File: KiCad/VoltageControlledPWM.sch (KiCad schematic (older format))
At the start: 26 parts, among them J1 +12V|GND|-12V, J2 3.3V|5.0V (Output Reference), J3 3.3V | 5.0V Voltage Control, J4 PWM Output, Q1 2N3906, U1 LM393, U2 CA3240E, U3 LM311

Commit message: Latest updates
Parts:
- added TP0: GND, TestPoint:TestPoint_Loop_D2.50mm_Drill1.0mm, symbol Connector:TestPoint
- added TP1: Square Wave, TestPoint:TestPoint_Loop_D2.50mm_Drill1.0mm, symbol Connector:TestPoint
- added TP2: Triange Wave, TestPoint:TestPoint_Loop_D2.50mm_Drill1.0mm, symbol Connector:TestPoint
- added TP3: Sweep, TestPoint:TestPoint_Loop_D2.50mm_Drill1.0mm, symbol Connector:TestPoint
- J1: value +12V|GND|-12V -> -12V | GND | +12V
- J2: value 3.3V|5.0V (Output Reference) -> 3.3V or 5.0V (Output Reference)
- J3: value 3.3V | 5.0V Voltage Control -> 3.3V or 5.0V Voltage Control
- R6: value 500 -> 460
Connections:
- net GND: now also TP0.1
- net at R1.1, R1.2, R3.3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: now also TP1.1
- net at C1.1, R2.1, U2.1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: now also TP2.1
- net at R10.1, U2.7, U3.2 (+): now also TP3.1
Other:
- moved on the sheet: C1, C2, C3, C4, C5, C6, C7, J1, J2, J3, J4, Q1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

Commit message: Updated to the board.
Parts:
- R8: value 20K -> 27K
- R9: value 5K -> 10K
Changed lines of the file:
@@
 Sheet 1 1
 Title "Voltage Controlled PWM"
-Date "2021-07-16"
+Date "2021-07-20"
 Rev "V1.0"
 Comp "TetraSys"
@@
 P 6200 5400
 F 0 "R8" H 6268 5446 50  0000 L CNN
-F 1 "20K" H 6268 5355 50  0000 L CNN
+F 1 "27K" H 6268 5355 50  0000 L CNN
 F 2 "Resistor_THT:R_Axial_DIN0207_L6.3mm_D2.5mm_P10.16mm_Horizontal" H 6200 5400 50  0001 C CNN
 F 3 "~" H 6200 5400 50  0001 C CNN
@@
 P 5900 5200
 F 0 "R9" V 5787 5200 50  0000 C CNN
-F 1 "5K" V 5696 5200 50  0000 C CNN
+F 1 "10K" V 5696 5200 50  0000 C CNN
 F 2 "Potentiometer_THT:Potentiometer_Bourns_3296W_Vertical" H 5900 5200 50  0001 C CNN
 F 3 "~" H 5900 5200 50  0001 C CNN
@@
 $EndComp
 $Comp
-L power:GND #PWR?
+L power:GND #PWR0106
 U 1 1 613AE6B3
 P 7800 4900
-F 0 "#PWR?" H 7800 4650 50  0001 C CNN
+F 0 "#PWR0106" H 7800 4650 50  0001 C CNN
 F 1 "GND" H 7805 4727 50  0000 C CNN
 F 2 "" H 7800 4900 50  0001 C CNN

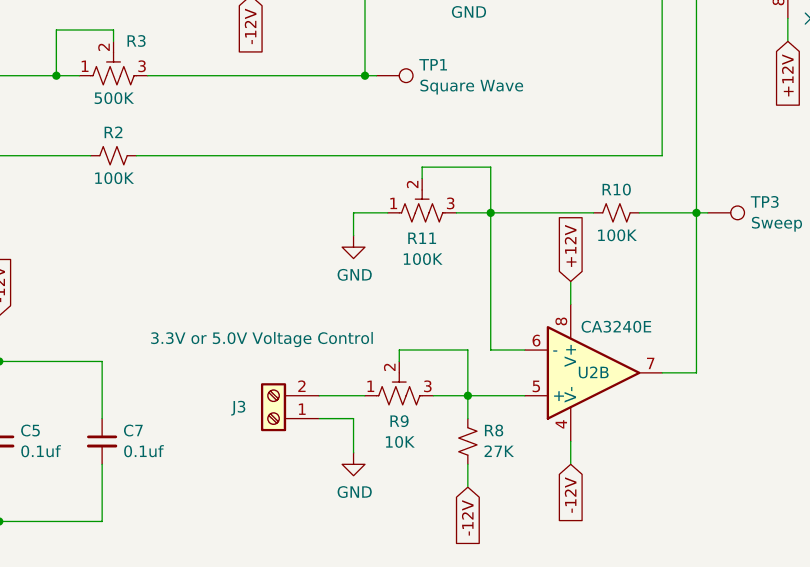
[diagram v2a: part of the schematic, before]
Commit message: Fixes for version 2.0. Changed the direction of increase voltage on R9 and R11. Increased silkscreen size of TPs.
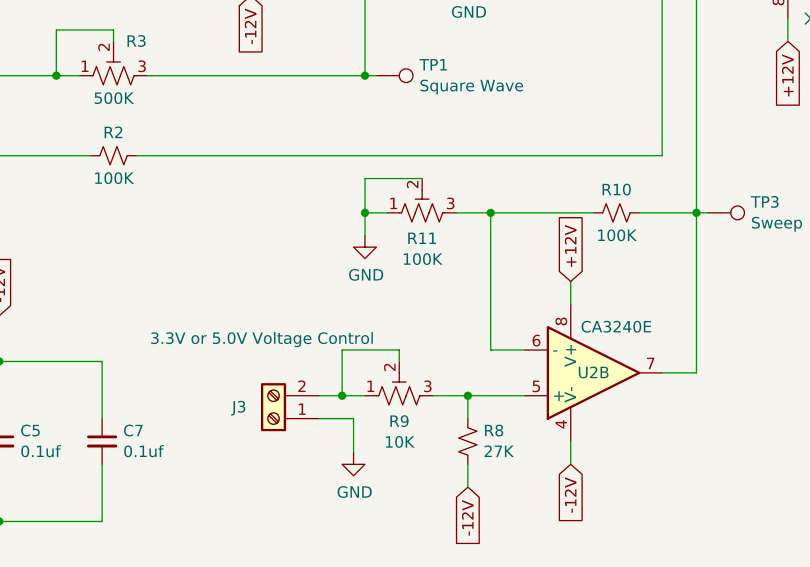
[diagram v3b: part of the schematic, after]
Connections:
- net GND: now also R11.2
- net at R8.1, R9.3, U2.5 (+): no longer R9.2
- net at R10.2, R11.3, U2.6 (-): no longer R11.2
- net at J3.2 (Pin_2), R9.1: now also R9.2
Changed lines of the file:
@@
 L power:GND #PWR0104
 U 1 1 60F706DC
-P 5700 4500
-F 0 "#PWR0104" H 5700 4250 50  0001 C CNN
-F 1 "GND" H 5705 4327 50  0000 C CNN
-F 2 "" H 5700 4500 50  0001 C CNN
-F 3 "" H 5700 4500 50  0001 C CNN
-	1    5700 4500
+P 5750 4500
+F 0 "#PWR0104" H 5750 4250 50  0001 C CNN
+F 1 "GND" H 5755 4327 50  0000 C CNN
+F 2 "" H 5750 4500 50  0001 C CNN
+F 3 "" H 5750 4500 50  0001 C CNN
+	1    5750 4500
 	1    0    0    -1
 $EndComp
@@
 	7050 3150 7400 3150
 Wire Wire Line
-	5850 4400 5700 4400
-Wire Wire Line
-	5700 4400 5700 4500
+	5850 4400 5750 4400
+Wire Wire Line
+	5750 4400 5750 4500
 Wire Wire Line
 	6200 5200 6200 5300
@@
 $EndComp
 Wire Wire Line
-	5550 5200 5750 5200
+	5550 5200 5650 5200
 Wire Wire Line
 	8200 3250 8350 3250
@@
 	0    -1   -1   0
 $EndComp
-Wire Wire Line
-	6000 4250 6000 4200
-Wire Wire Line
-	6000 4200 6300 4200
-Wire Wire Line
-	6300 4200 6300 4400
 $Comp
 L Device:R_POT_TRIM_US R9
@@
 Wire Wire Line
 	5900 5050 5900 5000
-Wire Wire Line
-	5900 5000 6200 5000
-Wire Wire Line
-	6200 5000 6200 5200
 Connection ~ 6200 5200
 Wire Wire Line
@@
 Wire Wire Line
 	7800 4800 7800 4900
+Connection ~ 5750 4400
+Wire Wire Line
+	5900 5000 5650 5000
+Wire Wire Line
+	5650 5000 5650 5200
+Connection ~ 5650 5200
+Wire Wire Line
+	5650 5200 5750 5200
+Wire Wire Line
+	5750 4250 5750 4400
+Wire Wire Line
+	5750 4250 6000 4250
 $EndSCHEMATC
